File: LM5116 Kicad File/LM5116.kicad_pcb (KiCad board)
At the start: 4 copper layers, 58.5 x 83.3 mm, 88 parts, among them J1 XT60-M, J10 PH1-01-UA, J11 PH1-01-UA, J12 PH1-01-UA, J13 PH1-01-UA, J14 61300311121, J15 61300311121, J16 61300311121, J17 61300311121, J18 61300311121, J19 61300311121, J2 PH1-01-UA, J20 61300311121, J21 61300311121, J22 61300311121, J23 61300311121, J24 61300311121, J25 61300311121, J3 PH1-01-UA, J4 PH1-01-UA, J5 PH1-01-UA, J6 PH1-01-UA, J7 PH1-01-UA, J8 PH1-01-UA, J9 PH1-01-UA, Q1 CSD17304Q3, Q2 CSD17304Q3, Q3 CSD17304Q3, Q4 CSD17304Q3, Q5 2N7002, Q6 IQDH29NE2LM5CG, U1 LM25116MHX/NOPB, U2 TLV1701AIDBVR, U3 TL431DBZ

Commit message: Update Kicad File
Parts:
- moved C1 5.08 mm to (147.9, 85.9)
- moved C10 5.08 mm to (144.1, 85.9)
- moved C13 5.08 mm to (135.1, 116.2)
- moved C15 5.08 mm to (121.8, 123.6)
- moved C18 5.08 mm to (158.6, 124.1)
- moved C19 5.08 mm to (128.1, 91.4)
- moved C21 5.08 mm to (138.7, 80.9)
- moved C4 5.08 mm to (158.7, 77.7)
- moved C6 5.08 mm to (134.5, 82.2)
- moved C8 5.08 mm to (130.7, 86.0)
- moved C9 5.08 mm to (142.8, 82.7)
- moved D1 5.08 mm to (134.5, 77.1)
- moved D3 5.08 mm to (144.7, 82.1)
- moved D4 5.08 mm to (166.4, 121.7)
- moved F1 5.08 mm to (138.3, 65.7)
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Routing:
- net GNDPWR: track 72.7 -> 68.7 mm
- net GND: track 13.4 -> 12.2 mm, vias 36 -> 71
- net /VOUT: track 212.5 -> 213.5 mm

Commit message: Upload inductor footprint
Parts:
- moved C11 10.3 mm to (160.0, 113.7)
- moved L2 7.84 mm to (160.7, 101.6), turned to 90 degrees
- moved J1 5.13 mm to (145.9, 62.1)
- moved L1 4.86 mm to (160.6, 89.0), turned to 90 degrees
- moved F1 4.53 mm to (133.9, 66.6)
- moved C13 2.67 mm to (135.1, 113.5)
- moved C12 2.28 mm to (147.2, 113.5)
- moved J14 1.01 mm to (168.1, 128.4)
- moved J15 1.01 mm to (163.7, 128.4)
- moved J16 1.01 mm to (159.3, 128.4)
- moved J17 1.01 mm to (154.8, 128.4)
- moved J18 1.01 mm to (150.4, 128.4)
- moved J19 1.01 mm to (145.9, 128.4)
- moved J20 1.01 mm to (141.5, 128.4)
- moved J21 1.01 mm to (137.0, 128.4)
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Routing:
- net GNDPWR: track 68.7 -> 55.9 mm
- net /SW: vias 38 -> 23
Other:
- board size 58.5 x 83.3 mm -> 58.5 x 78.8 mm

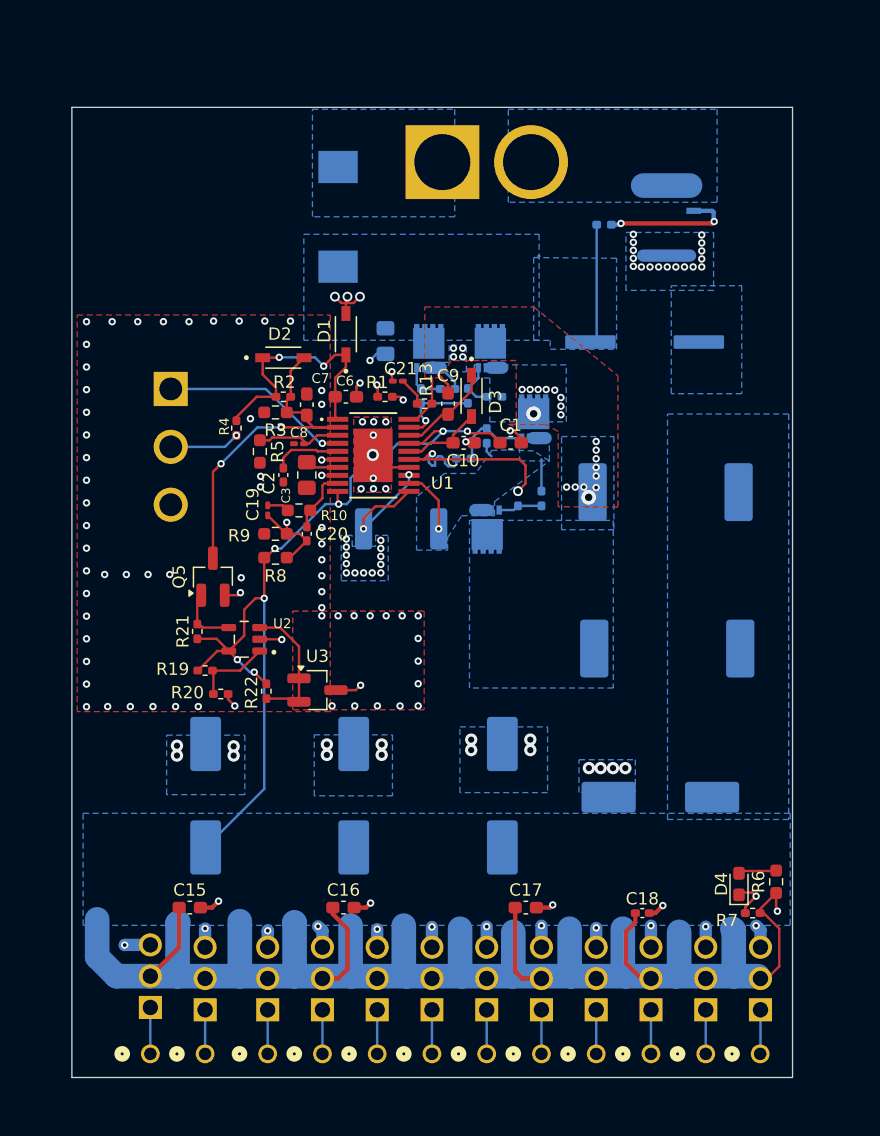
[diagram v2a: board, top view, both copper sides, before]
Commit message: Update inductor Footprint and 3D model
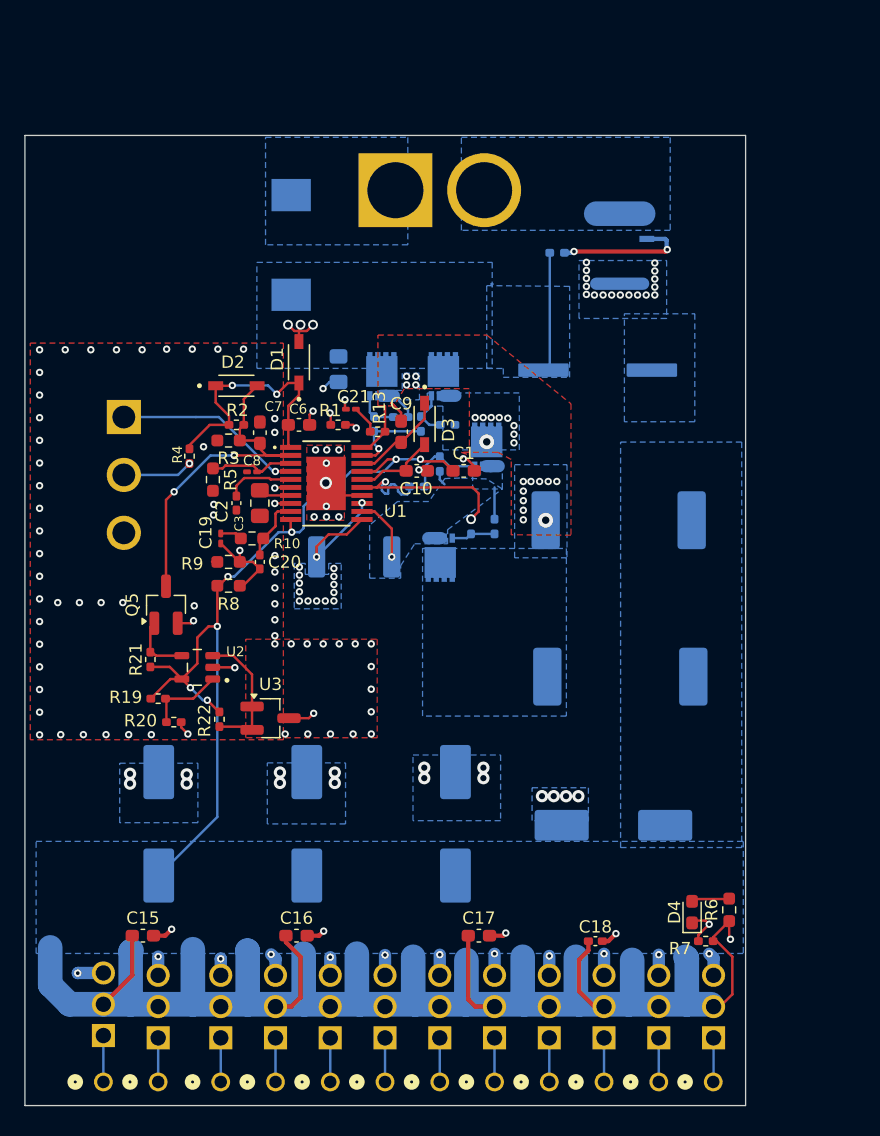
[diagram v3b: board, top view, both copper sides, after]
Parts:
- moved C2 4.44 mm to (125.6, 89.8)
- moved C20 4.44 mm to (127.5, 94.6)
- moved C3 4.44 mm to (127.5, 89.8)
- moved C7 4.44 mm to (127.5, 84.1)
- moved D2 4.44 mm to (125.6, 80.3)
- moved R2 4.44 mm to (125.6, 83.4)
- moved R22 4.44 mm to (124.2, 107.3)
- moved C1 4.44 mm to (144.1, 87.2)
- moved C10 4.44 mm to (140.2, 87.2)
- moved C18 4.44 mm to (154.7, 125.3)
- moved L2 4.44 mm to (156.8, 103.9)
- moved Q3 4.44 mm to (142.2, 94.2)
- moved R17 4.44 mm to (135.2, 94.2)
- moved R21 4.44 mm to (118.6, 102.5)
- moved R27 4.44 mm to (142.1, 86.6)
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
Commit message: Update Footprint
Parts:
- added J26: 691137710002, 691137710002:691137710002, B.Cu at (146.1, 60.3)
- moved J1 6.23 mm to (146.1, 69.2)
- moved R23 4.56 mm to (156.1, 70.5)
- moved D3 4.45 mm to (145.3, 83.4)
- moved D4 4.45 mm to (167.0, 123.0)
- moved J11 4.45 mm to (133.2, 136.8)
- moved J17 4.45 mm to (155.4, 130.7)
- moved J22 4.45 mm to (133.2, 130.7)
- moved J5 4.45 mm to (155.4, 136.8)
- moved R12 4.45 mm to (141.2, 83.4)
- moved R14 4.45 mm to (149.1, 91.7)
- moved R24 4.45 mm to (147.2, 83.4)
- moved R25 4.45 mm to (143.4, 82.8)
- moved U3 4.45 mm to (132.8, 107.2)
- moved C2 4.45 mm to (130.0, 89.8)
- moved C20 4.45 mm to (132.0, 94.6)
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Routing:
- net /SOURCE: track 13.6 -> 7.62 mm
- net Net-(Q6-GATE): track 10.9 -> 11.7 mm
- net GND: vias 71 -> 70
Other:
- board size 58.5 x 78.8 mm -> 58.5 x 83.5 mm
- board text added: "+"
- board text added: "-"

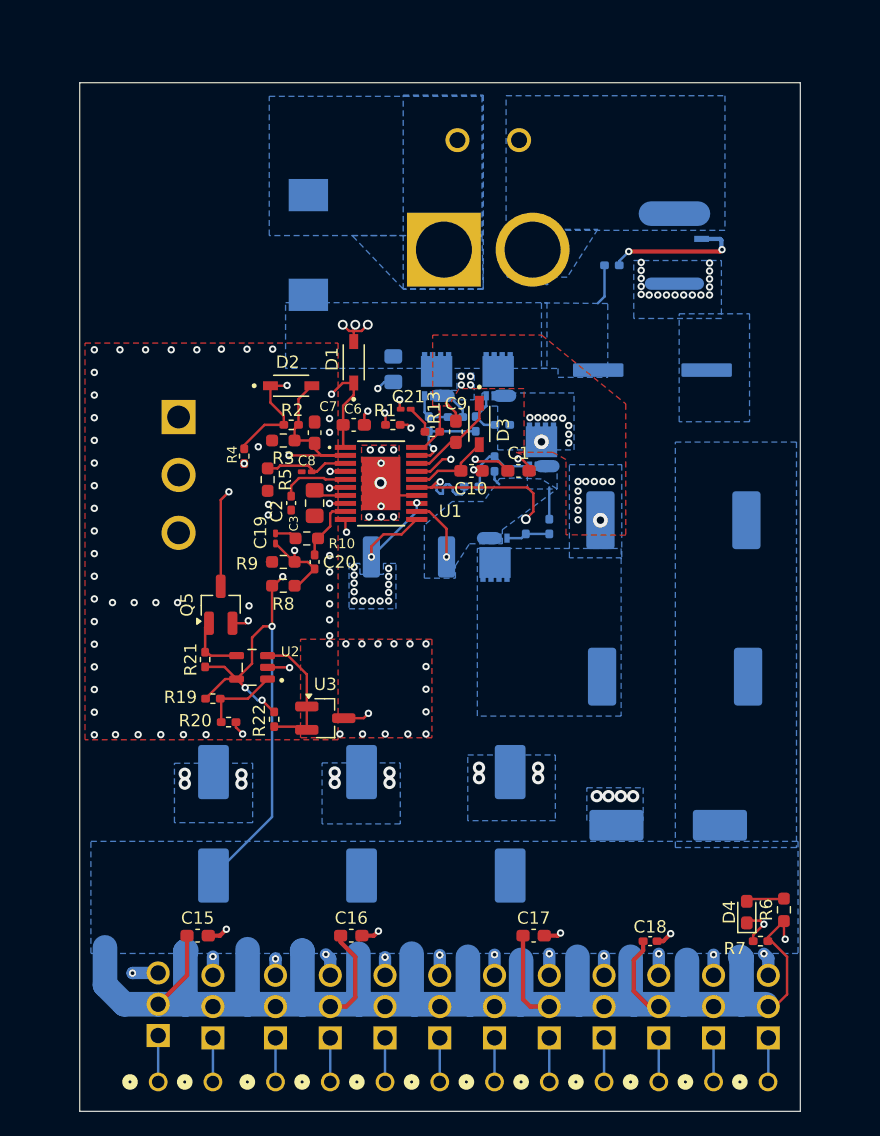
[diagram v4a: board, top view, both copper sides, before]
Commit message: Update Kicad footprint
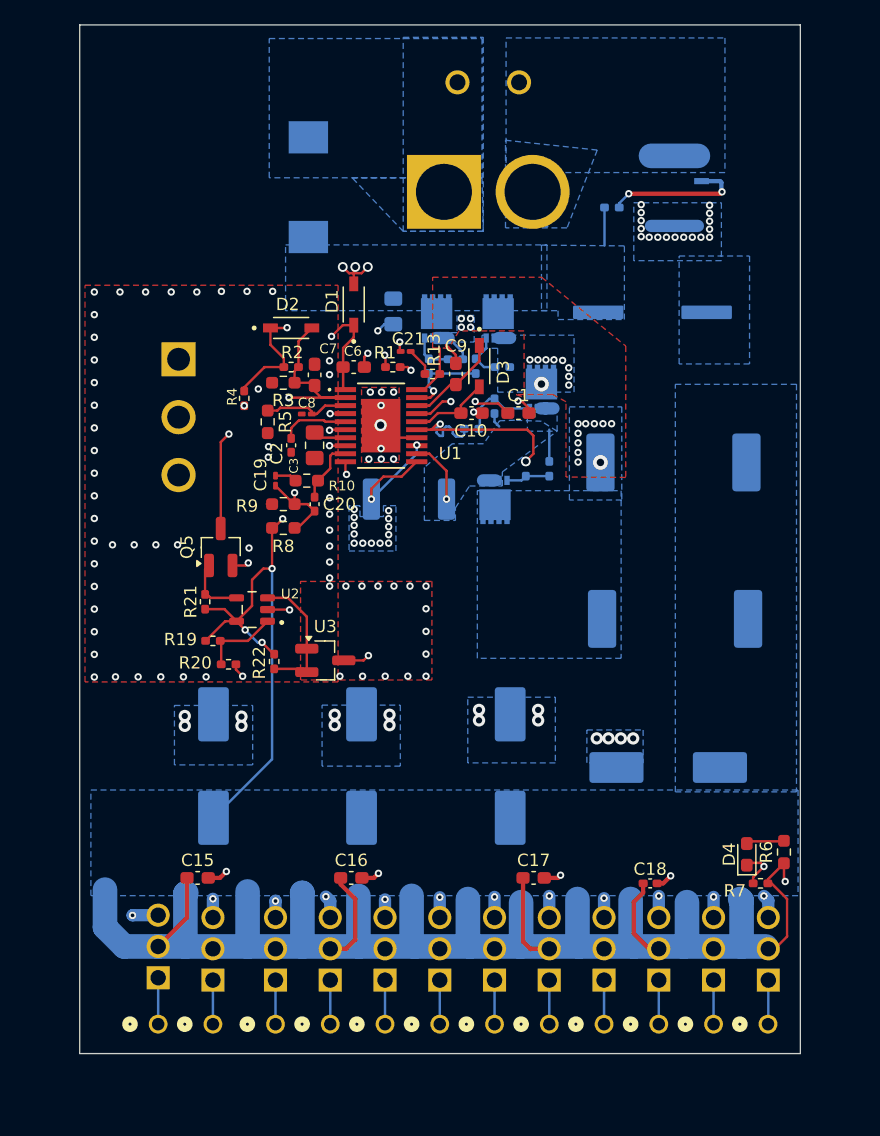
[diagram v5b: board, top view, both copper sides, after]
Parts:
- moved C9 4.69 mm to (143.4, 79.3)
- moved L2 4.69 mm to (161.3, 99.2)
- moved R13 4.69 mm to (141.5, 79.3)
- moved S1 4.69 mm to (120.9, 82.8)
- moved U1 4.69 mm to (137.3, 83.5)
- moved J26 4.69 mm to (146.1, 55.6)
- moved C1 4.69 mm to (148.5, 82.5)
- moved C10 4.69 mm to (144.7, 82.5)
- moved C11 4.69 mm to (160.7, 111.3)
- moved C12 4.69 mm to (147.8, 111.1)
- moved C13 4.69 mm to (135.8, 111.1)
- moved C14 4.69 mm to (123.7, 111.1)
- moved C15 4.69 mm to (122.5, 120.2)
- moved C16 4.69 mm to (134.9, 120.2)
- moved C17 4.69 mm to (149.7, 120.2)
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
